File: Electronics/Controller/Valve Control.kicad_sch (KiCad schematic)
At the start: 0 parts

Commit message: Working on schematic.
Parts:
- added J18: FRONT HEIGHT, symbol Connector_Generic:Conn_01x05
- added J19: REAR HEIGHT, symbol Connector_Generic:Conn_01x05
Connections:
- new net FRONT_DIR1: J18.5 (Pin_5)
- new net FRONT_DIR2: J18.3 (Pin_3)
- new net FRONT_PWM1: J18.4 (Pin_4)
- new net FRONT_PWM2: J18.2 (Pin_2)
- new net GND: J18.1 (Pin_1), J19.1 (Pin_1)
- new net REAR_DIR1: J19.5 (Pin_5)
- new net REAR_DIR2: J19.3 (Pin_3)
- new net REAR_PWM1: J19.4 (Pin_4)
- new net REAR_PWM2: J19.2 (Pin_2)
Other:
- note added: "CYTRON MDD10A"
- company: (none) -> (C) andy@britishideas.com 2025
- title: (none) -> Tandem Leveller Controller
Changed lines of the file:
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@@
 (kicad_sch (version 20230121) (generator eeschema)
   (paper "A4")
+  (title_block
+    (title "Tandem Leveller Controller")
+    (date "2025-02-16")
+    (rev "V1.0")
+    (company "(C) andy@britishideas.com 2025")
+    (comment 1 "For personal use only, no commercial use")
+    (comment 2 "Provided as-is, no warranty express or implied. Use at your own risk")
+  )
+  (junction (at 141.605 97.79) (diameter 0) (color 0 0 0 0)
+  )
+  (wire (pts (xy 134.62 80.645) (xy 147.32 80.645))
+    (stroke (width 0) (type default))
+  )
+  (wire (pts (xy 147.32 78.105) (xy 141.605 78.105))
+    (stroke (width 0) (type default))
+  )
+  (wire (pts (xy 134.62 105.41) (xy 147.32 105.41))
+    (stroke (width 0) (type default))
+  )
+  (wire (pts (xy 141.605 97.79) (xy 147.32 97.79))
+    (stroke (width 0) (type default))
+  )
+  (wire (pts (xy 141.605 78.105) (xy 141.605 97.79))
+    (stroke (width 0) (type default))
+  )
+  (wire (pts (xy 134.62 100.33) (xy 147.32 100.33))
+    (stroke (width 0) (type default))
+  )
+  (wire (pts (xy 134.62 102.87) (xy 147.32 102.87))
+    (stroke (width 0) (type default))
+  )
+  (wire (pts (xy 134.62 83.185) (xy 147.32 83.185))
+    (stroke (width 0) (type default))
+  )
+  (wire (pts (xy 134.62 107.95) (xy 147.32 107.95))
+    (stroke (width 0) (type default))
+  )
+  (wire (pts (xy 134.62 88.265) (xy 147.32 88.265))
+    (stroke (width 0) (type default))
+  )
+  (wire (pts (xy 134.62 85.725) (xy 147.32 85.725))
+    (stroke (width 0) (type default))
+  )
+  (wire (pts (xy 141.605 97.79) (xy 141.605 115.57))
+    (stroke (width 0) (type default))
+  )
+  (text "CYTRON MDD10A" (at 155.575 88.265 0)
+    (effects (font (size 1.27 1.27)) (justify left bottom))
+  )
+  (text "CYTRON MDD10A" (at 155.575 107.95 0)
+    (effects (font (size 1.27 1.27)) (justify left bottom))
+  )
+  (hierarchical_label "REAR_PWM1" (shape input) (at 134.62 105.41 180) (fields_autoplaced)
+    (effects (font (size 1.27 1.27)) (justify right))
+  )
+  (hierarchical_label "REAR_DIR1" (shape input) (at 134.62 107.95 180) (fields_autoplaced)
+    (effects (font (size 1.27 1.27)) (justify right))
+  )
+  (hierarchical_label "FRONT_DIR2" (shape input) (at 134.62 83.185 180) (fields_autoplaced)
+    (effects (font (size 1.27 1.27)) (justify right))
+  )
+  (hierarchical_label "FRONT_PWM1" (shape input) (at 134.62 85.725 180) (fields_autoplaced)
+    (effects (font (size 1.27 1.27)) (justify right))
+  )
+  (hierarchical_label "REAR_DIR2" (shape input) (at 134.62 102.87 180) (fields_autoplaced)
+    (effects (font (size 1.27 1.27)) (justify right))
+  )
+  (hierarchical_label "FRONT_PWM2" (shape input) (at 134.62 80.645 180) (fields_autoplaced)
+    (effects (font (size 1.27 1.27)) (justify right))
+  )
+  (hierarchical_label "REAR_PWM2" (shape input) (at 134.62 100.33 180) (fields_autoplaced)
+    (effects (font (size 1.27 1.27)) (justify right))
+  )
+  (hierarchical_label "FRONT_DIR1" (shape input) (at 134.62 88.265 180) (fields_autoplaced)
+    (effects (font (size 1.27 1.27)) (justify right))
+  )
+  (symbol (lib_id "Connector_Generic:Conn_01x05") (at 152.4 83.185 0) (unit 1)
+    (in_bom yes) (on_board yes) (dnp no) (fields_autoplaced)
+    (property "Reference" "J18" (at 155.575 81.915 0)
+      (effects (font (size 1.27 1.27)) (justify left))
+    )
+    (property "Value" "FRONT HEIGHT" (at 155.575 84.455 0)
+      (effects (font (size 1.27 1.27)) (justify left))
+    )
+    (property "Footprint" "" (at 152.4 83.185 0)
+      (effects (font (size 1.27 1.27)) hide)
+    )
+    (property "Datasheet" "~" (at 152.4 83.185 0)
+      (effects (font (size 1.27 1.27)) hide)
+    )
+    (pin "1")
+    (pin "2")
+    (pin "4")
+    (pin "5")
+    (pin "3")
+    (instances
+      (project "Tandem Leveller Controller"
+        (path "/56ffd1a6-bbed-43b6-8aa8-f23f49f76448/9e68b822-6469-4f83-b3f9-7a42b55305fd"
+          (reference "J18") (unit 1)
+        )
+      )
+    )
+  )
+  (symbol (lib_id "power:GND") (at 141.605 115.57 0) (unit 1)
+    (in_bom yes) (on_board yes) (dnp no) (fields_autoplaced)
+    (property "Reference" "#PWR084" (at 141.605 121.92 0)
+      (effects (font (size 1.27 1.27)) hide)
+    )
+    (property "Value" "GND" (at 141.605 120.015 0)
+      (effects (font (size 1.27 1.27)))
+    )
+    (property "Footprint" "" (at 141.605 115.57 0)
+      (effects (font (size 1.27 1.27)) hide)
+    )
+    (property "Datasheet" "" (at 141.605 115.57 0)
+      (effects (font (size 1.27 1.27)) hide)
+    )
+    (pin "1")
+    (instances
+      (project "Tandem Leveller Controller"
+        (path "/56ffd1a6-bbed-43b6-8aa8-f23f49f76448/9e68b822-6469-4f83-b3f9-7a42b55305fd"
+          (reference "#PWR084") (unit 1)
+        )
+      )
+    )
+  )
+  (symbol (lib_id "Connector_Generic:Conn_01x05") (at 152.4 102.87 0) (unit 1)
+    (in_bom yes) (on_board yes) (dnp no) (fields_autoplaced)
+    (property "Reference" "J19" (at 155.575 101.6 0)
+      (effects (font (size 1.27 1.27)) (justify left))
+    )
+    (property "Value" "REAR HEIGHT" (at 155.575 104.14 0)
+      (effects (font (size 1.27 1.27)) (justify left))
+    )
+    (property "Footprint" "" (at 152.4 102.87 0)
+      (effects (font (size 1.27 1.27)) hide)
+    )
+    (property "Datasheet" "~" (at 152.4 102.87 0)
+      (effects (font (size 1.27 1.27)) hide)
+    )
+    (pin "1")
+    (pin "2")
+    (pin "4")
+    (pin "5")
+    (pin "3")
+    (instances
+      (project "Tandem Leveller Controller"
+        (path "/56ffd1a6-bbed-43b6-8aa8-f23f49f76448/9e68b822-6469-4f83-b3f9-7a42b55305fd"
+          (reference "J19") (unit 1)
+        )
+      )
+    )
+  )
 )

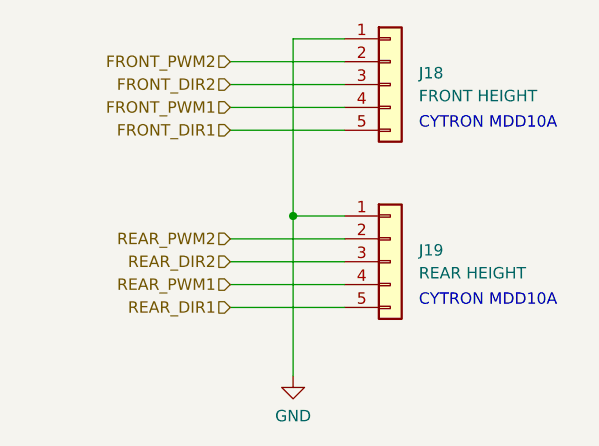
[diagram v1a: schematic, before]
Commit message: Updated schematic. Added footprints for all components.
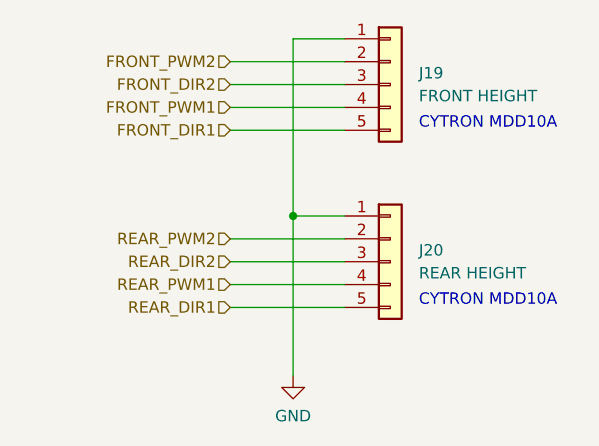
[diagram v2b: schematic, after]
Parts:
- J19: renamed from J18; footprint (none) -> Connector_JST:JST_PH_B5B-PH-K_1x05_P2.00mm_Vertical; manf# (none) -> B5B-PH-K-S
- J20: renamed from J19; footprint (none) -> Connector_JST:JST_PH_B5B-PH-K_1x05_P2.00mm_Vertical; manf# (none) -> B5B-PH-K-S
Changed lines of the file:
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@@
   (symbol (lib_id "Connector_Generic:Conn_01x05") (at 152.4 83.185 0) (unit 1)
     (in_bom yes) (on_board yes) (dnp no) (fields_autoplaced)
-    (property "Reference" "J18" (at 155.575 81.915 0)
+    (property "Reference" "J19" (at 155.575 81.915 0)
       (effects (font (size 1.27 1.27)) (justify left))
     )
@@
       (effects (font (size 1.27 1.27)) (justify left))
     )
-    (property "Footprint" "" (at 152.4 83.185 0)
+    (property "Footprint" "Connector_JST:JST_PH_B5B-PH-K_1x05_P2.00mm_Vertical" (at 152.4 83.185 0)
       (effects (font (size 1.27 1.27)) hide)
     )
     (property "Datasheet" "~" (at 152.4 83.185 0)
+      (effects (font (size 1.27 1.27)) hide)
+    )
+    (property "manf#" "B5B-PH-K-S" (at 152.4 83.185 0)
+      (effects (font (size 1.27 1.27)) hide)
+    )
+    (property "Field5" "" (at 152.4 83.185 0)
       (effects (font (size 1.27 1.27)) hide)
     )
@@
       (project "Tandem Leveller Controller"
         (path "/56ffd1a6-bbed-43b6-8aa8-f23f49f76448/9e68b822-6469-4f83-b3f9-7a42b55305fd"
-          (reference "J18") (unit 1)
+          (reference "J19") (unit 1)
         )
       )
@@
   (symbol (lib_id "power:GND") (at 141.605 115.57 0) (unit 1)
     (in_bom yes) (on_board yes) (dnp no) (fields_autoplaced)
-    (property "Reference" "#PWR084" (at 141.605 121.92 0)
+    (property "Reference" "#PWR086" (at 141.605 121.92 0)
       (effects (font (size 1.27 1.27)) hide)
     )
@@
       (project "Tandem Leveller Controller"
         (path "/56ffd1a6-bbed-43b6-8aa8-f23f49f76448/9e68b822-6469-4f83-b3f9-7a42b55305fd"
-          (reference "#PWR084") (unit 1)
+          (reference "#PWR086") (unit 1)
         )
       )
@@
   (symbol (lib_id "Connector_Generic:Conn_01x05") (at 152.4 102.87 0) (unit 1)
     (in_bom yes) (on_board yes) (dnp no) (fields_autoplaced)
-    (property "Reference" "J19" (at 155.575 101.6 0)
+    (property "Reference" "J20" (at 155.575 101.6 0)
       (effects (font (size 1.27 1.27)) (justify left))
     )
@@
       (effects (font (size 1.27 1.27)) (justify left))
     )
-    (property "Footprint" "" (at 152.4 102.87 0)
+    (property "Footprint" "Connector_JST:JST_PH_B5B-PH-K_1x05_P2.00mm_Vertical" (at 152.4 102.87 0)
       (effects (font (size 1.27 1.27)) hide)
     )
     (property "Datasheet" "~" (at 152.4 102.87 0)
+      (effects (font (size 1.27 1.27)) hide)
+    )
+    (property "manf#" "B5B-PH-K-S" (at 152.4 102.87 0)
       (effects (font (size 1.27 1.27)) hide)
     )
@@
       (project "Tandem Leveller Controller"
         (path "/56ffd1a6-bbed-43b6-8aa8-f23f49f76448/9e68b822-6469-4f83-b3f9-7a42b55305fd"
-          (reference "J19") (unit 1)
+          (reference "J20") (unit 1)
         )
       )

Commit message: Changed switches and lamps. Removed status LEDs. Working on PCB layout.
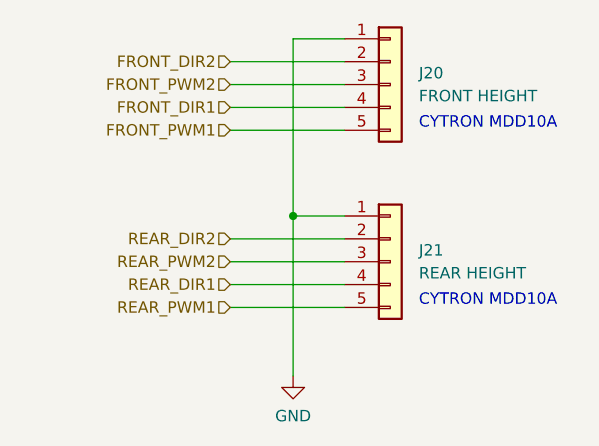
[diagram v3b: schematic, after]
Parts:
- renumbered J19 to J20, J20 to J21
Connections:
- net FRONT_DIR1: now also J20.4 (Pin_4); no longer J20.5 (Pin_5)
- net FRONT_DIR2: now also J20.2 (Pin_2); no longer J20.3 (Pin_3)
- net FRONT_PWM1: now also J20.5 (Pin_5); no longer J20.4 (Pin_4)
- net FRONT_PWM2: now also J20.3 (Pin_3); no longer J20.2 (Pin_2)
- net REAR_DIR1: now also J21.4 (Pin_4); no longer J21.5 (Pin_5)
- net REAR_DIR2: now also J21.2 (Pin_2); no longer J21.3 (Pin_3)
- net REAR_PWM1: now also J21.5 (Pin_5); no longer J21.4 (Pin_4)
- net REAR_PWM2: now also J21.3 (Pin_3); no longer J21.2 (Pin_2)
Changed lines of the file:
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@@
   (title_block
     (title "Tandem Leveller Controller")
-    (date "2025-02-16")
+    (date "2025-02-18")
     (rev "V1.0")
     (company "(C) andy@britishideas.com 2025")
@@
     (effects (font (size 1.27 1.27)) (justify left bottom))
   )
-  (hierarchical_label "REAR_PWM1" (shape input) (at 134.62 105.41 180) (fields_autoplaced)
+  (hierarchical_label "REAR_PWM1" (shape input) (at 134.62 107.95 180) (fields_autoplaced)
     (effects (font (size 1.27 1.27)) (justify right))
   )
-  (hierarchical_label "REAR_DIR1" (shape input) (at 134.62 107.95 180) (fields_autoplaced)
+  (hierarchical_label "REAR_DIR1" (shape input) (at 134.62 105.41 180) (fields_autoplaced)
     (effects (font (size 1.27 1.27)) (justify right))
   )
-  (hierarchical_label "FRONT_DIR2" (shape input) (at 134.62 83.185 180) (fields_autoplaced)
+  (hierarchical_label "FRONT_DIR2" (shape input) (at 134.62 80.645 180) (fields_autoplaced)
     (effects (font (size 1.27 1.27)) (justify right))
   )
-  (hierarchical_label "FRONT_PWM1" (shape input) (at 134.62 85.725 180) (fields_autoplaced)
+  (hierarchical_label "FRONT_PWM1" (shape input) (at 134.62 88.265 180) (fields_autoplaced)
     (effects (font (size 1.27 1.27)) (justify right))
   )
-  (hierarchical_label "REAR_DIR2" (shape input) (at 134.62 102.87 180) (fields_autoplaced)
+  (hierarchical_label "REAR_DIR2" (shape input) (at 134.62 100.33 180) (fields_autoplaced)
     (effects (font (size 1.27 1.27)) (justify right))
   )
-  (hierarchical_label "FRONT_PWM2" (shape input) (at 134.62 80.645 180) (fields_autoplaced)
+  (hierarchical_label "FRONT_PWM2" (shape input) (at 134.62 83.185 180) (fields_autoplaced)
     (effects (font (size 1.27 1.27)) (justify right))
   )
-  (hierarchical_label "REAR_PWM2" (shape input) (at 134.62 100.33 180) (fields_autoplaced)
+  (hierarchical_label "REAR_PWM2" (shape input) (at 134.62 102.87 180) (fields_autoplaced)
     (effects (font (size 1.27 1.27)) (justify right))
   )
-  (hierarchical_label "FRONT_DIR1" (shape input) (at 134.62 88.265 180) (fields_autoplaced)
+  (hierarchical_label "FRONT_DIR1" (shape input) (at 134.62 85.725 180) (fields_autoplaced)
     (effects (font (size 1.27 1.27)) (justify right))
   )
   (symbol (lib_id "Connector_Generic:Conn_01x05") (at 152.4 83.185 0) (unit 1)
     (in_bom yes) (on_board yes) (dnp no) (fields_autoplaced)
-    (property "Reference" "J19" (at 155.575 81.915 0)
+    (property "Reference" "J20" (at 155.575 81.915 0)
       (effects (font (size 1.27 1.27)) (justify left))
     )
@@
       (project "Tandem Leveller Controller"
         (path "/56ffd1a6-bbed-43b6-8aa8-f23f49f76448/9e68b822-6469-4f83-b3f9-7a42b55305fd"
-          (reference "J19") (unit 1)
+          (reference "J20") (unit 1)
         )
       )
@@
   (symbol (lib_id "power:GND") (at 141.605 115.57 0) (unit 1)
     (in_bom yes) (on_board yes) (dnp no) (fields_autoplaced)
-    (property "Reference" "#PWR086" (at 141.605 121.92 0)
+    (property "Reference" "#PWR083" (at 141.605 121.92 0)
       (effects (font (size 1.27 1.27)) hide)
     )
@@
       (project "Tandem Leveller Controller"
         (path "/56ffd1a6-bbed-43b6-8aa8-f23f49f76448/9e68b822-6469-4f83-b3f9-7a42b55305fd"
-          (reference "#PWR086") (unit 1)
+          (reference "#PWR083") (unit 1)
         )
       )
@@
   (symbol (lib_id "Connector_Generic:Conn_01x05") (at 152.4 102.87 0) (unit 1)
     (in_bom yes) (on_board yes) (dnp no) (fields_autoplaced)
-    (property "Reference" "J20" (at 155.575 101.6 0)
+    (property "Reference" "J21" (at 155.575 101.6 0)
       (effects (font (size 1.27 1.27)) (justify left))
     )
@@
       (project "Tandem Leveller Controller"
         (path "/56ffd1a6-bbed-43b6-8aa8-f23f49f76448/9e68b822-6469-4f83-b3f9-7a42b55305fd"
-          (reference "J20") (unit 1)
+          (reference "J21") (unit 1)
         )
       )
